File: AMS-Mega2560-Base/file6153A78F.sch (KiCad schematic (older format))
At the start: 12 parts, among them Q2 IRF510, Q3 IRF510, Q4 IRF510, Q5 2N7000, Q6 2N7000

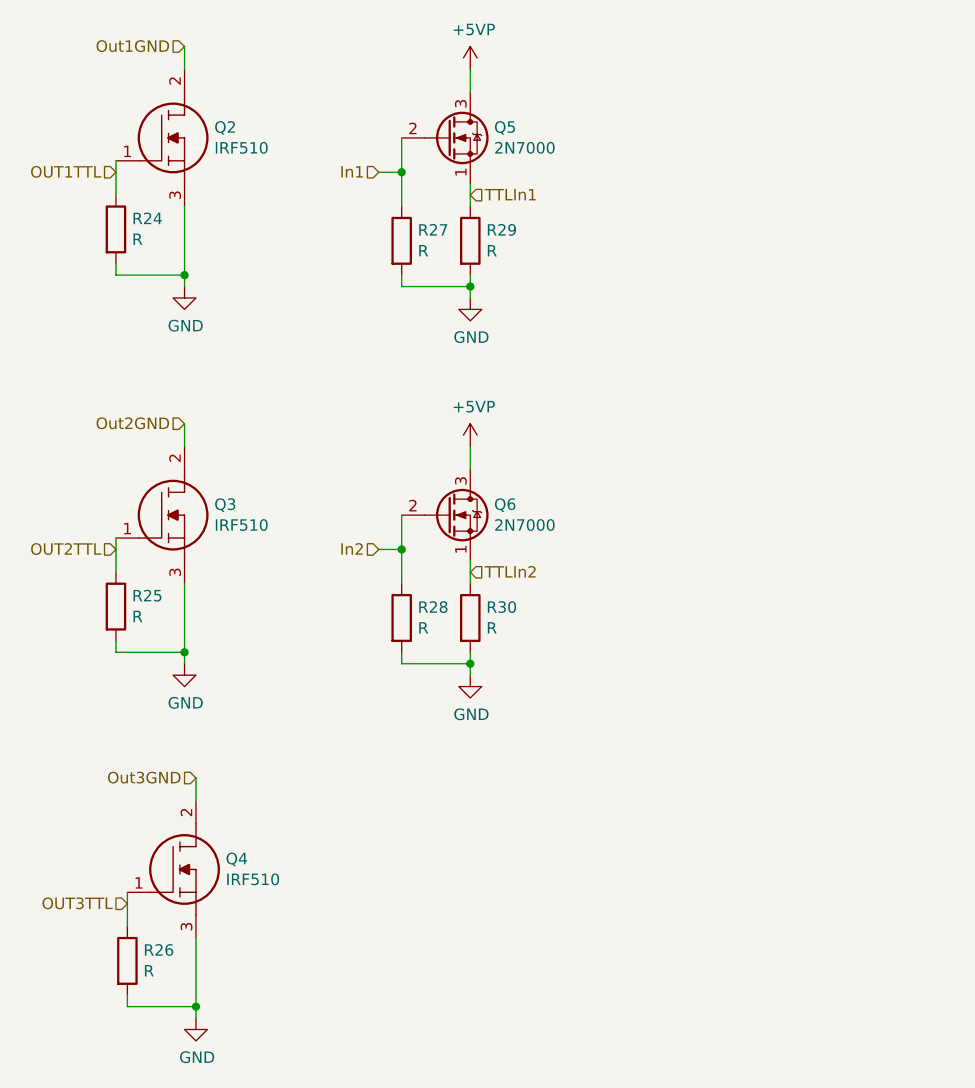
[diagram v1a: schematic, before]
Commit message: upgrading this to 6.0 and moving the vacuum sensors to a daughter board project.
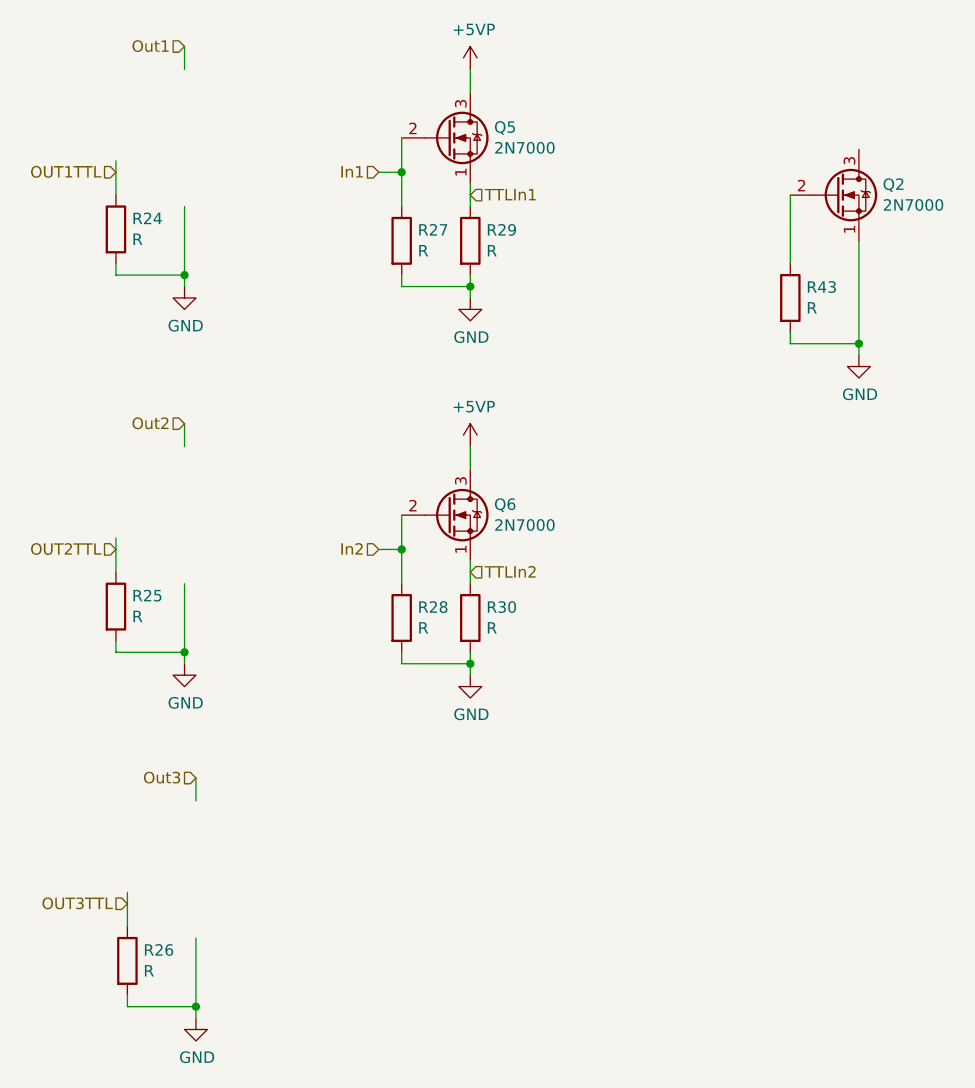
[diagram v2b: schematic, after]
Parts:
- removed Q2, Q3, Q4: IRF510, SamacSys_Parts:TO254P465X1024X2050-3P, symbol SamacSys_Parts:IRF510
- added Q2: 2N7000, Package_TO_SOT_THT:TO-92_Inline, symbol Transistor_FET:2N7000
- added R43: R, Resistor_THT:R_Axial_DIN0207_L6.3mm_D2.5mm_P5.08mm_Vertical, symbol Device:R
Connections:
- net labels added: Out1, Out2, Out3
- net labels removed: Out1GND, Out2GND, Out3GND
- wire segments 36 -> 41
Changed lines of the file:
@@
 $EndDescr
-$Comp
-L SamacSys_Parts:IRF510 Q?
-U 1 1 6151FB60
-P 4300 5150
-AR Path="/6153A790/6151FB60" Ref="Q?"  Part="1"
-AR Path="/623D3962/6151FB60" Ref="Q4"  Part="1"
-F 0 "Q4" H 4730 5296 50  0000 L CNN
-F 1 "IRF510" H 4730 5205 50  0000 L CNN
-F 2 "SamacSys_Parts:TO254P465X1024X2050-3P" H 4750 5100 50  0001 L CNN
-F 3 "https://www.vishay.com/docs/91015/sihf510.pdf" H 4750 5000 50  0001 L CNN
-F 4 "MOSFET RECOMMENDED ALT 844-IRF510PBF" H 4750 4900 50  0001 L CNN "Description"
-F 5 "4.65" H 4750 4800 50  0001 L CNN "Height"
-F 6 "844-IRF510" H 4750 4700 50  0001 L CNN "Mouser Part Number"
-F 7 "https://www.mouser.co.uk/ProductDetail/Vishay-Siliconix/IRF510?qs=ehM%252BESVsXgwwPzb18JjqFw%3D%3D" H 4750 4600 50  0001 L CNN "Mouser Price/Stock"
-F 8 "Vishay" H 4750 4500 50  0001 L CNN "Manufacturer_Name"
-F 9 "IRF510" H 4750 4400 50  0001 L CNN "Manufacturer_Part_Number"
-	1    4300 5150
-	1    0    0    -1
-$EndComp
 $Comp
 L Device:R R?
@@
 P 4600 5700
 AR Path="/6153A790/615214D7" Ref="#PWR?"  Part="1"
-AR Path="/623D3962/615214D7" Ref="#PWR097"  Part="1"
-F 0 "#PWR097" H 4600 5450 50  0001 C CNN
+AR Path="/623D3962/615214D7" Ref="#PWR098"  Part="1"
+F 0 "#PWR098" H 4600 5450 50  0001 C CNN
 F 1 "GND" H 4605 5527 50  0000 C CNN
 F 2 "" H 4600 5700 50  0001 C CNN
@@
 	4300 5150 4300 5300
 Text HLabel 4600 4650 0    50   Input ~ 0
-Out3GND
+Out3
 Text HLabel 4300 5200 0    50   Input ~ 0
 OUT3TTL
 Wire Wire Line
 	4600 4750 4600 4650
-$Comp
-L SamacSys_Parts:IRF510 Q?
-U 1 1 623FCDC8
-P 4250 3600
-AR Path="/6153A790/623FCDC8" Ref="Q?"  Part="1"
-AR Path="/623D3962/623FCDC8" Ref="Q3"  Part="1"
-F 0 "Q3" H 4680 3746 50  0000 L CNN
-F 1 "IRF510" H 4680 3655 50  0000 L CNN
-F 2 "SamacSys_Parts:TO254P465X1024X2050-3P" H 4700 3550 50  0001 L CNN
-F 3 "https://www.vishay.com/docs/91015/sihf510.pdf" H 4700 3450 50  0001 L CNN
-F 4 "MOSFET RECOMMENDED ALT 844-IRF510PBF" H 4700 3350 50  0001 L CNN "Description"
-F 5 "4.65" H 4700 3250 50  0001 L CNN "Height"
-F 6 "844-IRF510" H 4700 3150 50  0001 L CNN "Mouser Part Number"
-F 7 "https://www.mouser.co.uk/ProductDetail/Vishay-Siliconix/IRF510?qs=ehM%252BESVsXgwwPzb18JjqFw%3D%3D" H 4700 3050 50  0001 L CNN "Mouser Price/Stock"
-F 8 "Vishay" H 4700 2950 50  0001 L CNN "Manufacturer_Name"
-F 9 "IRF510" H 4700 2850 50  0001 L CNN "Manufacturer_Part_Number"
-	1    4250 3600
-	1    0    0    -1
-$EndComp
 $Comp
 L Device:R R?
@@
 P 4550 4150
 AR Path="/6153A790/623FCDD5" Ref="#PWR?"  Part="1"
-AR Path="/623D3962/623FCDD5" Ref="#PWR096"  Part="1"
-F 0 "#PWR096" H 4550 3900 50  0001 C CNN
+AR Path="/623D3962/623FCDD5" Ref="#PWR097"  Part="1"
+F 0 "#PWR097" H 4550 3900 50  0001 C CNN
 F 1 "GND" H 4555 3977 50  0000 C CNN
 F 2 "" H 4550 4150 50  0001 C CNN
@@
 	4250 3600 4250 3750
 Text HLabel 4550 3100 0    50   Input ~ 0
-Out2GND
+Out2
 Text HLabel 4250 3650 0    50   Input ~ 0
 OUT2TTL
@@
 P 5800 4200
 AR Path="/6153A790/623FCDF6" Ref="#PWR?"  Part="1"
-AR Path="/623D3962/623FCDF6" Ref="#PWR0101"  Part="1"
-F 0 "#PWR0101" H 5800 3950 50  0001 C CNN
+AR Path="/623D3962/623FCDF6" Ref="#PWR0102"  Part="1"
+F 0 "#PWR0102" H 5800 3950 50  0001 C CNN
 F 1 "GND" H 5805 4027 50  0000 C CNN
 F 2 "" H 5800 4200 50  0001 C CNN
@@
 AR Path="/61493C0E/623FCE08" Ref="#PWR?"  Part="1"
 AR Path="/6153A790/623FCE08" Ref="#PWR?"  Part="1"
-AR Path="/623D3962/623FCE08" Ref="#PWR0100"  Part="1"
-F 0 "#PWR0100" H 5800 3050 50  0001 C CNN
+AR Path="/623D3962/623FCE08" Ref="#PWR0101"  Part="1"
+F 0 "#PWR0101" H 5800 3050 50  0001 C CNN
 F 1 "+5VP" H 5815 3373 50  0000 C CNN
 F 2 "" H 5800 3200 50  0001 C CNN
 F 3 "" H 5800 3200 50  0001 C CNN
 	1    5800 3200
-	1    0    0    -1
-$EndComp
-$Comp
-L SamacSys_Parts:IRF510 Q?
-U 1 1 623FFB6C
-P 4250 1950
-AR Path="/6153A790/623FFB6C" Ref="Q?"  Part="1"
-AR Path="/623D3962/623FFB6C" Ref="Q2"  Part="1"
-F 0 "Q2" H 4680 2096 50  0000 L CNN
-F 1 "IRF510" H 4680 2005 50  0000 L CNN
-F 2 "SamacSys_Parts:TO254P465X1024X2050-3P" H 4700 1900 50  0001 L CNN
-F 3 "https://www.vishay.com/docs/91015/sihf510.pdf" H 4700 1800 50  0001 L CNN
-F 4 "MOSFET RECOMMENDED ALT 844-IRF510PBF" H 4700 1700 50  0001 L CNN "Description"
-F 5 "4.65" H 4700 1600 50  0001 L CNN "Height"
-F 6 "844-IRF510" H 4700 1500 50  0001 L CNN "Mouser Part Number"
-F 7 "https://www.mouser.co.uk/ProductDetail/Vishay-Siliconix/IRF510?qs=ehM%252BESVsXgwwPzb18JjqFw%3D%3D" H 4700 1400 50  0001 L CNN "Mouser Price/Stock"
-F 8 "Vishay" H 4700 1300 50  0001 L CNN "Manufacturer_Name"
-F 9 "IRF510" H 4700 1200 50  0001 L CNN "Manufacturer_Part_Number"
-	1    4250 1950
 	1    0    0    -1
 $EndComp
@@
 P 4550 2500
 AR Path="/6153A790/623FFB79" Ref="#PWR?"  Part="1"
-AR Path="/623D3962/623FFB79" Ref="#PWR095"  Part="1"
-F 0 "#PWR095" H 4550 2250 50  0001 C CNN
+AR Path="/623D3962/623FFB79" Ref="#PWR096"  Part="1"
+F 0 "#PWR096" H 4550 2250 50  0001 C CNN
 F 1 "GND" H 4555 2327 50  0000 C CNN
 F 2 "" H 4550 2500 50  0001 C CNN
@@
 	4250 1950 4250 2100
 Text HLabel 4550 1450 0    50   Input ~ 0
-Out1GND
+Out1
 Text HLabel 4250 2000 0    50   Input ~ 0
 OUT1TTL
@@
 P 5800 2550
 AR Path="/6153A790/623FFB9A" Ref="#PWR?"  Part="1"
-AR Path="/623D3962/623FFB9A" Ref="#PWR099"  Part="1"
-F 0 "#PWR099" H 5800 2300 50  0001 C CNN
+AR Path="/623D3962/623FFB9A" Ref="#PWR0100"  Part="1"
+F 0 "#PWR0100" H 5800 2300 50  0001 C CNN
 F 1 "GND" H 5805 2377 50  0000 C CNN
 F 2 "" H 5800 2550 50  0001 C CNN
@@
 AR Path="/61493C0E/623FFBAC" Ref="#PWR?"  Part="1"
 AR Path="/6153A790/623FFBAC" Ref="#PWR?"  Part="1"
-AR Path="/623D3962/623FFBAC" Ref="#PWR098"  Part="1"
-F 0 "#PWR098" H 5800 1400 50  0001 C CNN
+AR Path="/623D3962/623FFBAC" Ref="#PWR099"  Part="1"
+F 0 "#PWR099" H 5800 1400 50  0001 C CNN
 F 1 "+5VP" H 5815 1723 50  0000 C CNN
 F 2 "" H 5800 1550 50  0001 C CNN
@@
 	1    0    0    -1
 $EndComp
+$Comp
+L Transistor_FET:2N7000 Q2
+U 1 1 6175F336
+P 7400 2100
+F 0 "Q2" H 7604 2146 50  0000 L CNN
+F 1 "2N7000" H 7604 2055 50  0000 L CNN
+F 2 "Package_TO_SOT_THT:TO-92_Inline" H 7600 2025 50  0001 L CIN
+F 3 "https://www.onsemi.com/pub/Collateral/NDS7002A-D.PDF" H 7400 2100 50  0001 L CNN
+	1    7400 2100
+	1    0    0    -1
+$EndComp
+$Comp
+L Device:R R?
+U 1 1 6176136D
+P 7200 2550
+AR Path="/6153A790/6176136D" Ref="R?"  Part="1"
+AR Path="/623D3962/6176136D" Ref="R43"  Part="1"
+F 0 "R43" H 7270 2596 50  0000 L CNN
+F 1 "R" H 7270 2505 50  0000 L CNN
+F 2 "Resistor_THT:R_Axial_DIN0207_L6.3mm_D2.5mm_P5.08mm_Vertical" V 7130 2550 50  0001 C CNN
+F 3 "~" H 7200 2550 50  0001 C CNN
+	1    7200 2550
+	1    0    0    -1
+$EndComp
+Wire Wire Line
+	7500 2800 7500 2750
+$Comp
+L power:GND #PWR?
+U 1 1 61761374
+P 7500 2800
+AR Path="/6153A790/61761374" Ref="#PWR?"  Part="1"
+AR Path="/623D3962/61761374" Ref="#PWR086"  Part="1"
+F 0 "#PWR086" H 7500 2550 50  0001 C CNN
+F 1 "GND" H 7505 2627 50  0000 C CNN
+F 2 "" H 7500 2800 50  0001 C CNN
+F 3 "" H 7500 2800 50  0001 C CNN
+	1    7500 2800
+	1    0    0    -1
+$EndComp
+Wire Wire Line
+	7200 2700 7200 2750
+Wire Wire Line
+	7200 2750 7500 2750
+Connection ~ 7500 2750
+Wire Wire Line
+	7500 2300 7500 2750
+Wire Wire Line
+	7200 2100 7200 2400
 $EndSCHEMATC
